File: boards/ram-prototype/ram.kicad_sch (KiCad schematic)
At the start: 29 parts, among them J1 SRAM_Bus

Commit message: Update schematic with new row/col architecture
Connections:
- net Address Decoder/A2 renamed Column Select/A2
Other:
- removed sheet Read OE Gen
- removed sheet Write Clk Gen
- added sheet Column Select (column_select.kicad_sch)
- added sheet Read Enable Gen (read_en_gen.kicad_sch)
- added sheet Write Enable Gen (write_en_gen.kicad_sch)
- sheet Address Decoder ports: added ROW_SEL_0, ROW_SEL_1, ROW_SEL_2, ROW_SEL_3; removed A2, SEL0, SEL1, SEL2, SEL3, SEL4, SEL5, SEL6, SEL7
- sheet Byte 0 ports: added COL_SEL, READ_EN_ROW, WRITE_EN_ROW; removed BUF_OE, WRITE_CLK
- sheet Byte 1 ports: added COL_SEL, READ_EN_ROW, WRITE_EN_ROW; removed BUF_OE, WRITE_CLK
- sheet Byte 2 ports: added COL_SEL, READ_EN_ROW, WRITE_EN_ROW; removed BUF_OE, WRITE_CLK
- sheet Byte 3 ports: added COL_SEL, READ_EN_ROW, WRITE_EN_ROW; removed BUF_OE, WRITE_CLK
- sheet Byte 4 ports: added COL_SEL, READ_EN_ROW, WRITE_EN_ROW; removed BUF_OE, WRITE_CLK
- sheet Byte 5 ports: added COL_SEL, READ_EN_ROW, WRITE_EN_ROW; removed BUF_OE, WRITE_CLK
- sheet Byte 6 ports: added COL_SEL, READ_EN_ROW, WRITE_EN_ROW; removed BUF_OE, WRITE_CLK
- sheet Byte 7 ports: added COL_SEL, READ_EN_ROW, WRITE_EN_ROW; removed BUF_OE, WRITE_CLK

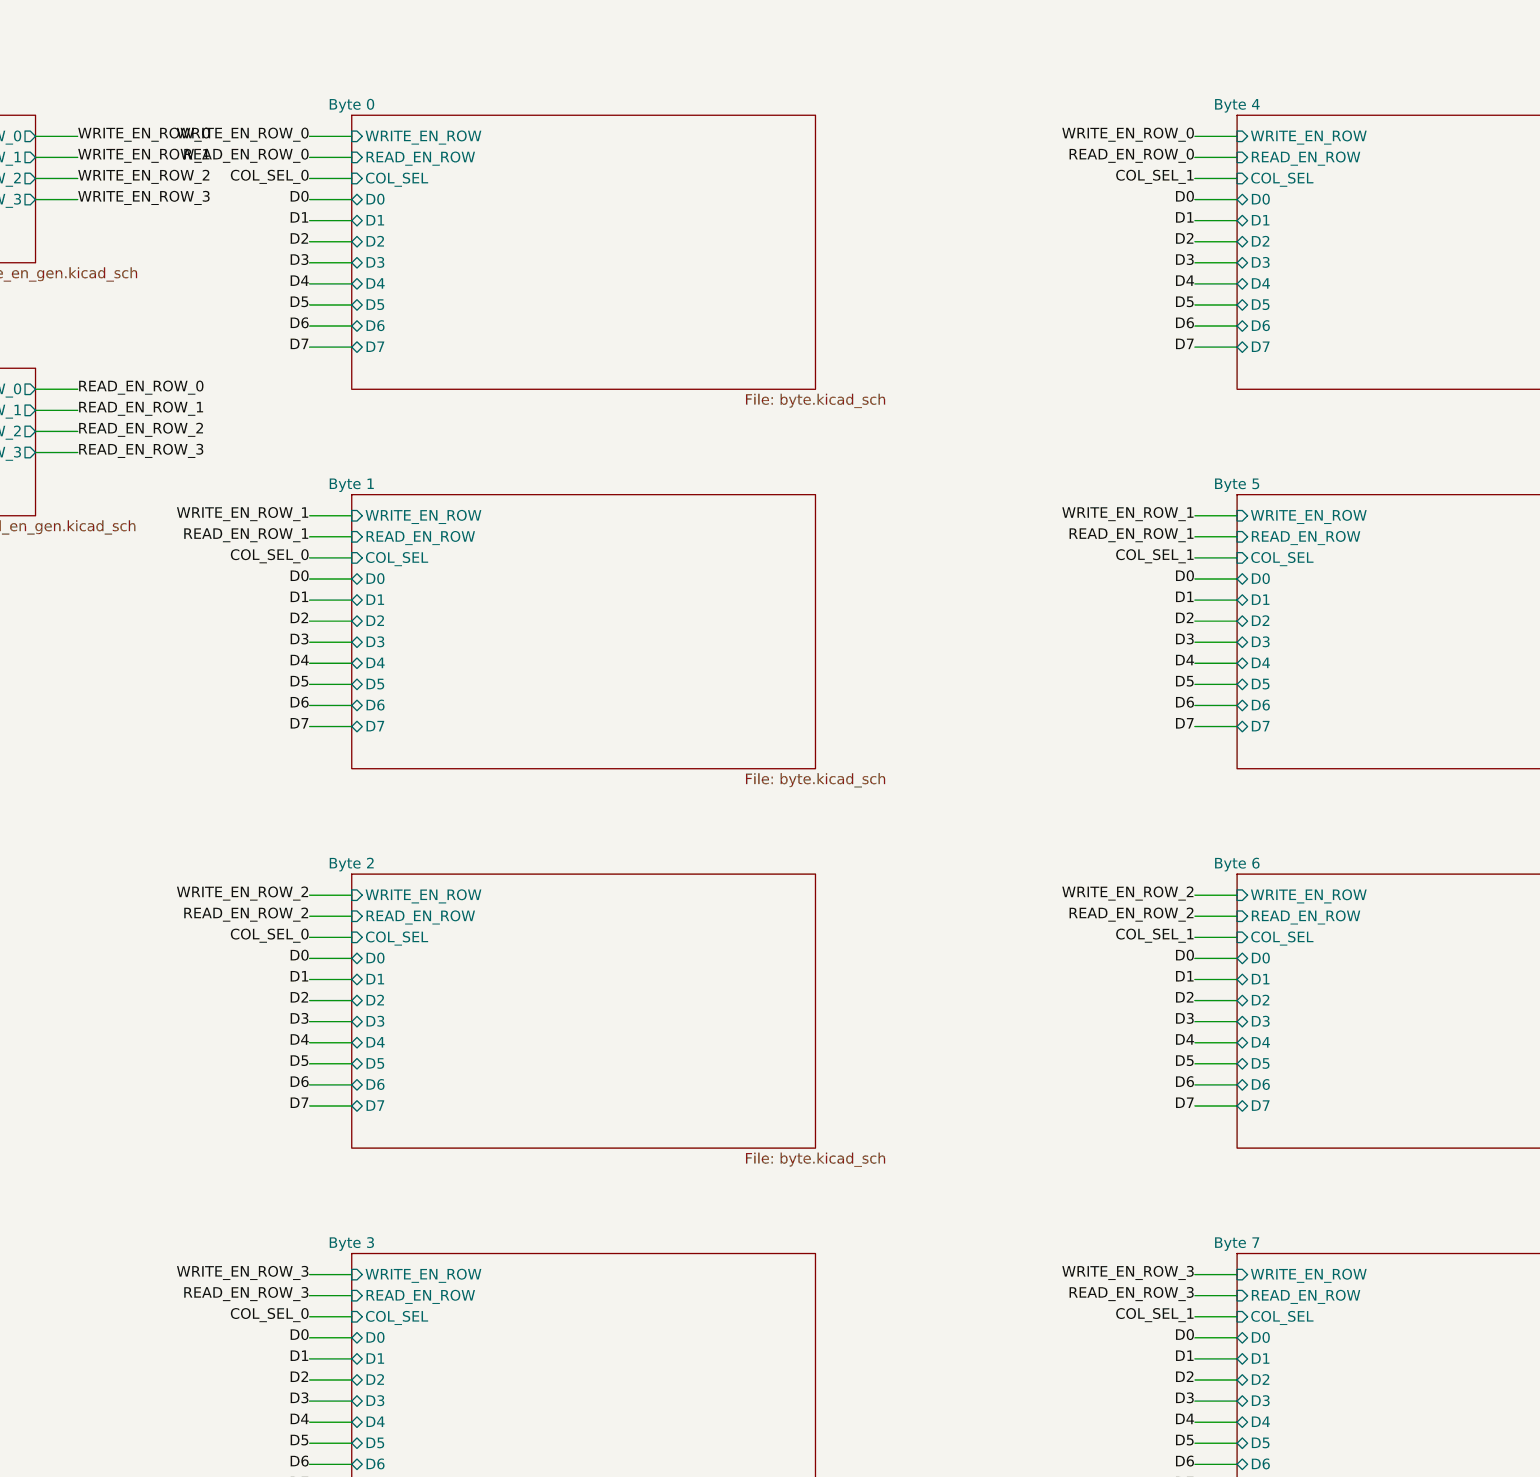
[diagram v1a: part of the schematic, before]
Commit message: route column selects
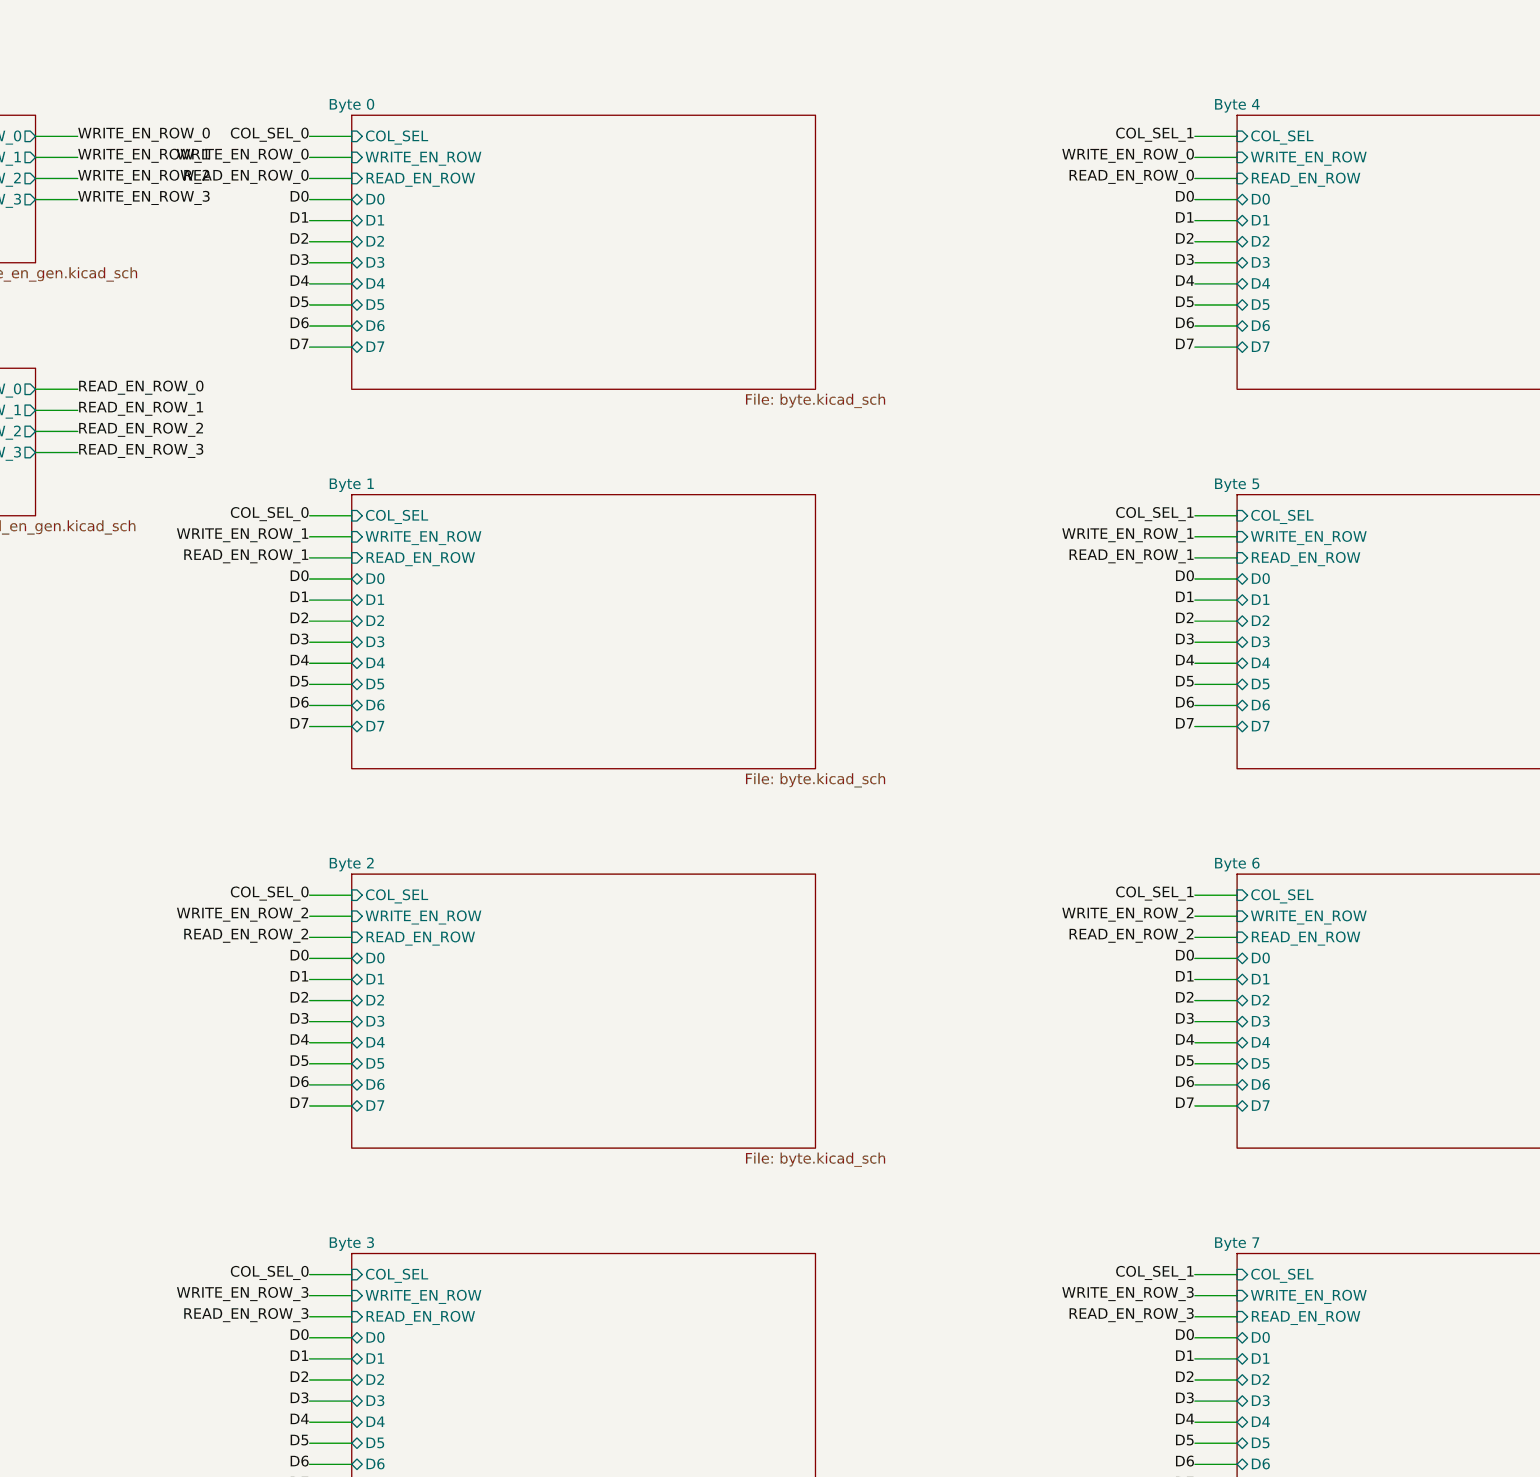
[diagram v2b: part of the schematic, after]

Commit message: Change layout
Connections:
- net Address Decoder/A0: now also D5.2 (A), J1.11 (Pin_11); no longer D1.2 (A), J1.15 (Pin_15)
- net Address Decoder/A1: now also D4.2 (A), J1.12 (Pin_12); no longer D2.2 (A), J1.14 (Pin_14)
- net Column Select/A2: now also D14.2 (A), J1.2 (Pin_2); no longer D3.2 (A), J1.13 (Pin_13)
- net Control Logic/nCE: now also D3.2 (A), J1.13 (Pin_13); no longer D6.2 (A), J1.10 (Pin_10)
- net Control Logic/nOE: now also D1.2 (A), J1.15 (Pin_15); no longer D4.2 (A), J1.12 (Pin_12)
- net Control Logic/nWE: now also D2.2 (A), J1.14 (Pin_14); no longer D5.2 (A), J1.11 (Pin_11)
- net D0: now also D6.2 (A), J1.10 (Pin_10); no longer D7.2 (A), J1.9 (Pin_9)
- net D1: now also D7.2 (A), J1.9 (Pin_9); no longer D8.2 (A), J1.8 (Pin_8)
- net D2: now also D8.2 (A), J1.8 (Pin_8); no longer D9.2 (A), J1.7 (Pin_7)
- net D3: now also D9.2 (A), J1.7 (Pin_7); no longer D10.2 (A), J1.6 (Pin_6)
- net D4: now also D10.2 (A), J1.6 (Pin_6); no longer D11.2 (A), J1.5 (Pin_5)
- net D5: now also D11.2 (A), J1.5 (Pin_5); no longer D12.2 (A), J1.4 (Pin_4)
- net D6: now also D12.2 (A), J1.4 (Pin_4); no longer D13.2 (A), J1.3 (Pin_3)
- net D7: now also D13.2 (A), J1.3 (Pin_3); no longer D14.2 (A), J1.2 (Pin_2)

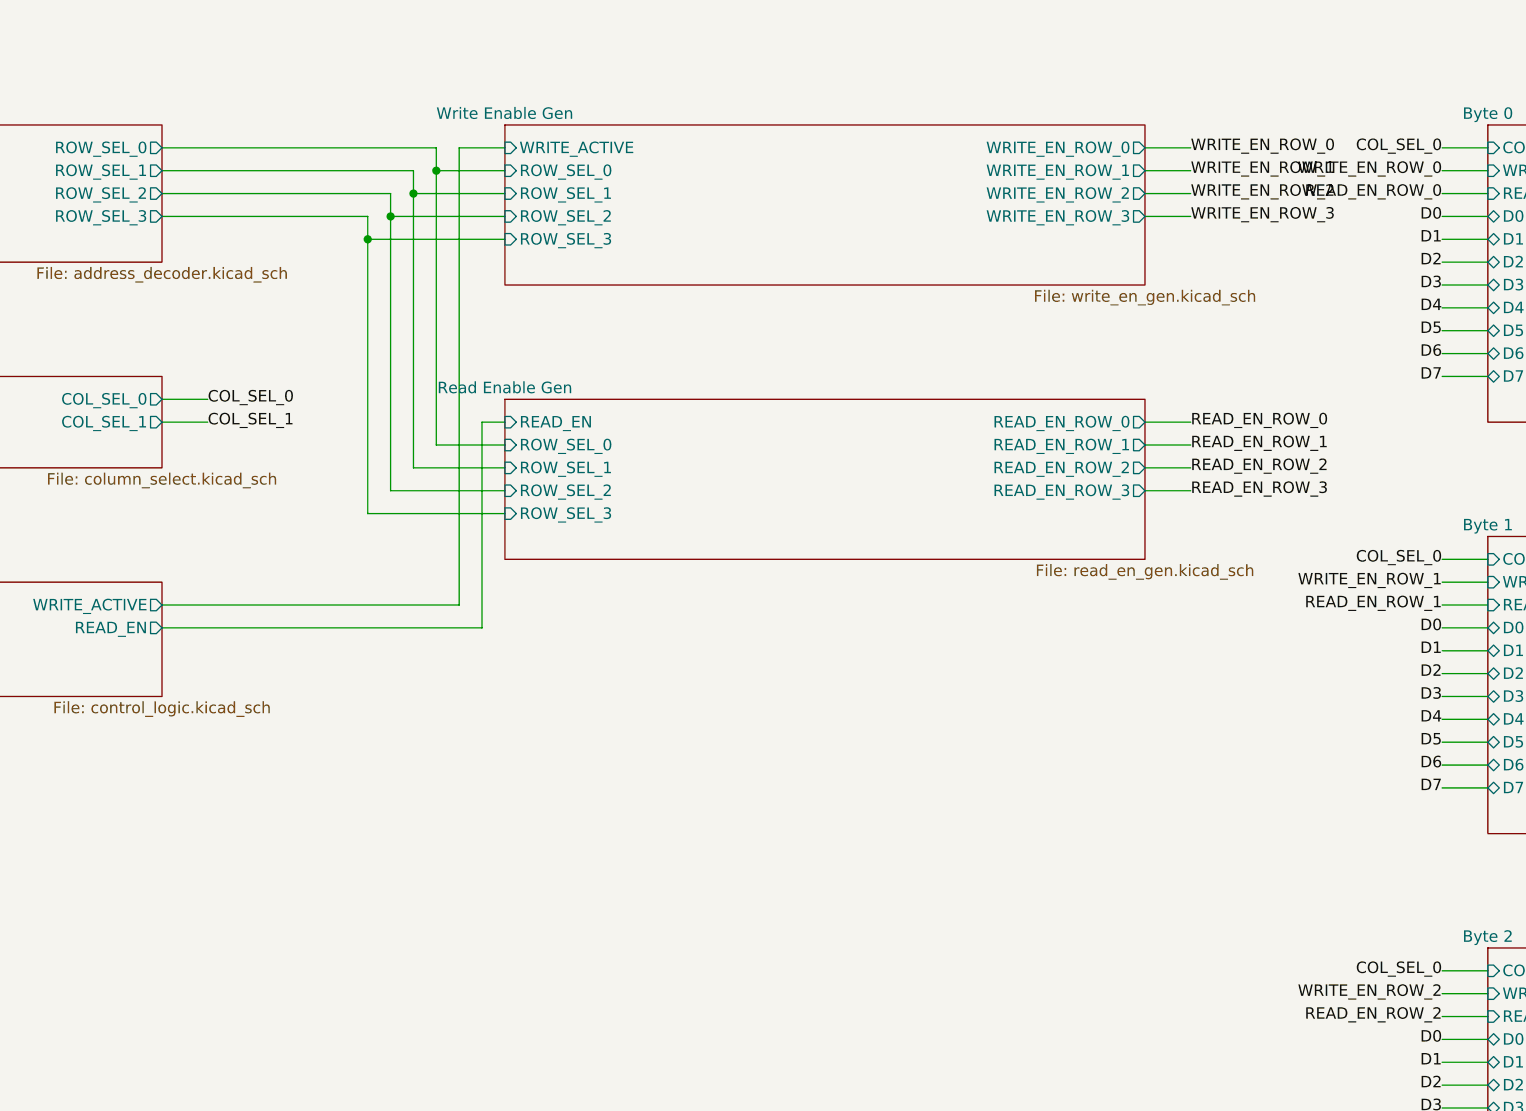
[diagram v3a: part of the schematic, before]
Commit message: refactor read and write schematics into row control sheets
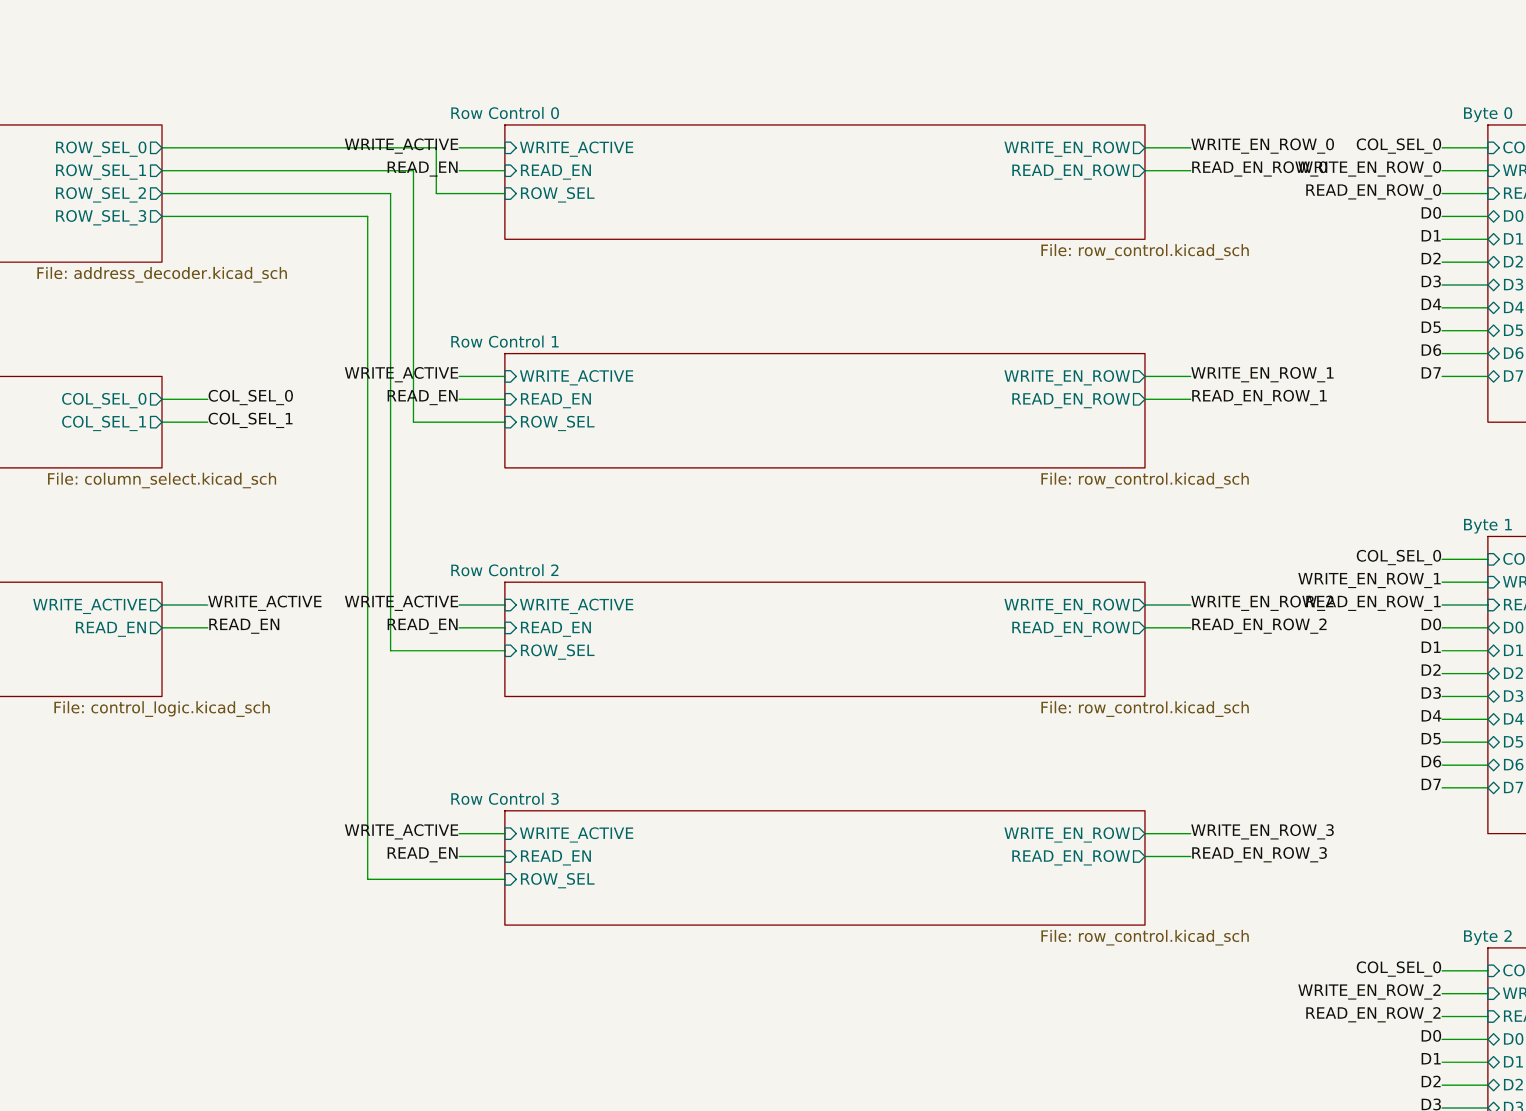
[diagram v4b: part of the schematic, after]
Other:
- removed sheet Read Enable Gen
- removed sheet Write Enable Gen
- added sheet Row Control 0 (row_control.kicad_sch)
- added sheet Row Control 1 (row_control.kicad_sch)
- added sheet Row Control 2 (row_control.kicad_sch)
- added sheet Row Control 3 (row_control.kicad_sch)

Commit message: Add initial changes to make logic close to final
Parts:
- removed J1: SRAM_Bus, symbol Connector_Generic:Conn_01x16
- added D15, D16, D17, D18, D19, D20, D21, D22: Red, symbol Device:LED_Small
- added J1: SRAM_Bus, symbol Connector_Generic:Conn_01x24
- added J2: Probe, symbol Connector_Generic:Conn_01x12
- added J3: Unused_COL_SEL, symbol Connector_Generic:Conn_01x14
- added R15, R16, R17, R18, R19, R20, R21, R22: 680R, symbol Device:R_Small
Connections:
- net Column Select/A2 is gone; now on net D3: D14.2 (A)
- net Address Decoder/A0: now also D10.2 (A), J1.14 (Pin_14); no longer D5.2 (A)
- net Address Decoder/A1: now also D9.2 (A), J1.15 (Pin_15); no longer D4.2 (A)
- net Control Logic/nCE: now also J1.21 (Pin_21)
- net Control Logic/nOE: now also J1.23 (Pin_23)
- net Control Logic/nWE: now also J1.22 (Pin_22)
- net D0: now also D11.2 (A), J1.13 (Pin_13); no longer D6.2 (A)
- net D1: now also D12.2 (A), J1.12 (Pin_12); no longer D7.2 (A)
- net D2: now also D13.2 (A), J1.11 (Pin_11); no longer D8.2 (A)
- net D3: now also J1.10 (Pin_10); no longer D9.2 (A)
- net D4: now also D15.2 (A), J1.9 (Pin_9); no longer D10.2 (A)
- net D5: now also D16.2 (A), J1.8 (Pin_8); no longer D11.2 (A)
- net D6: now also D17.2 (A), J1.7 (Pin_7); no longer D12.2 (A)
- net D7: now also D18.2 (A), J1.6 (Pin_6); no longer D13.2 (A)
- net GND: now also J1.1 (Pin_1), R15.2, R16.2, R17.2, R18.2, R19.2, R20.2, R21.2, R22.2
- net VCC: now also J1.24 (Pin_24)
- new net: D19.1 (K), R19.1
- new net: D17.1 (K), R17.1
- new net: D22.1 (K), R22.1
- new net: D18.1 (K), R18.1
- new net: D21.1 (K), R21.1
- new net: D15.1 (K), R15.1
- new net: D16.1 (K), R16.1
- new net: D20.1 (K), R20.1
- new net Address Decoder/A2: D8.2 (A), J1.16 (Pin_16)
- new net Address Decoder/A3: D7.2 (A), J1.17 (Pin_17)
- new net Address Decoder/A4: D6.2 (A), J1.18 (Pin_18)
- new net Address Decoder/A5: D5.2 (A), J1.19 (Pin_19)
- new net Address Decoder/A6: D4.2 (A), J1.20 (Pin_20)
- new net COL_SEL_10: J3.9 (Pin_9)
- new net COL_SEL_11: J3.10 (Pin_10)
- new net COL_SEL_12: J3.11 (Pin_11)
- new net COL_SEL_13: J3.12 (Pin_12)
- new net COL_SEL_14: J3.13 (Pin_13)
- new net COL_SEL_15: J3.14 (Pin_14)
- new net COL_SEL_2: J3.1 (Pin_1)
- new net COL_SEL_3: J3.2 (Pin_2)
- new net COL_SEL_4: J3.3 (Pin_3)
- new net COL_SEL_5: J3.4 (Pin_4)
- new net COL_SEL_6: J3.5 (Pin_5)
- new net COL_SEL_7: J3.6 (Pin_6)
- new net COL_SEL_8: J3.7 (Pin_7)
- new net COL_SEL_9: J3.8 (Pin_8)
- new net Column Select/A10: D19.2 (A), J1.5 (Pin_5)
- new net Column Select/A7: D22.2 (A), J1.2 (Pin_2)
- new net Column Select/A8: D21.2 (A), J1.3 (Pin_3)
- new net Column Select/A9: D20.2 (A), J1.4 (Pin_4)
- new net GA0: J2.5 (Pin_5)
- new net GA1: J2.6 (Pin_6)
- new net GA2: J2.7 (Pin_7)
- new net GA3: J2.8 (Pin_8)
- new net GB0: J2.9 (Pin_9)
- new net GB1: J2.10 (Pin_10)
- new net GB2: J2.11 (Pin_11)
- new net GB3: J2.12 (Pin_12)
- new net RS1: J2.1 (Pin_1)
- new net RS2: J2.2 (Pin_2)
- new net RS3: J2.3 (Pin_3)
- new net RS4: J2.4 (Pin_4)
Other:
- sheet Address Decoder ports: added A2, A3, A4, A5, A6, RS1, RS2, RS3, RS4; removed none
- sheet Column Select ports: added A10, A7, A8, A9, COL_SEL_10, COL_SEL_11, COL_SEL_12, COL_SEL_13, COL_SEL_14, COL_SEL_15, COL_SEL_2, COL_SEL_3, COL_SEL_4, COL_SEL_5, COL_SEL_6, COL_SEL_7, COL_SEL_8, COL_SEL_9, GA0, GA1, GA2, GA3, GB0, GB1, GB2, GB3; removed A2

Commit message: clean up
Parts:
- removed J2: Probe, symbol Connector_Generic:Conn_01x12
- added J2: Probe, symbol Connector_Generic:Conn_01x04
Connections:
- net RS1: now also J2.1 (Pin_1)
- net RS2: now also J2.2 (Pin_2)
- net RS3: now also J2.3 (Pin_3)
- net RS4: now also J2.4 (Pin_4)
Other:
- sheet Column Select ports: added none; removed GA0, GA1, GA2, GA3, GB0, GB1, GB2, GB3
